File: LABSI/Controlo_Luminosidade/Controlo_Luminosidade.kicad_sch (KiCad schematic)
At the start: 45 parts, among them J1 Barrel_Jack_Switch, J10 Touch Button, J11 Touch Button, J12 Touch Button, J2 Barrel_Jack_Switch, J3 Conn_01x05_Pin, J4 Conn_01x04_Pin, J5 Conn_01x04_Pin, J6 AVR-ISP-6, J7 Conn_01x03_Pin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

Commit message: pcb finalizado, gee«rbers gerados, falta desenvolver o que falta no ultimo commit
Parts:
- added J13: ESP32, Connector_PinSocket_2.54mm:PinSocket_1x04_P2.54mm_Vertical, symbol Connector_Generic:Conn_01x04
- added R8: 6.8k, Resistor_THT:R_Axial_DIN0204_L3.6mm_D1.6mm_P5.08mm_Horizontal, symbol Device:R
- added R9: 10k, Resistor_THT:R_Axial_DIN0204_L3.6mm_D1.6mm_P5.08mm_Horizontal, symbol Device:R
- C9: footprint Capacitor_THT:C_Disc_D3.0mm_W2.0mm_P2.50mm -> (none); now left out of the parts list
- R2: value 330 -> 220
- R4, R5, U2, U3: now left out of the parts list
- U4: footprint Connector_PinHeader_2.54mm:PinHeader_2x02_P2.54mm_Vertical -> Connector_PinSocket_2.54mm:PinSocket_2x02_P2.54mm_Vertical
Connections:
- net +5V: now also J13.3 (Pin_3)
- net GND: now also J13.4 (Pin_4), R9.2
- net TRIG: now also U1.25 (PC2); no longer U1.2 (PD0)
- net TRIG2: now also U1.26 (PC3); no longer U1.3 (PD1)
- net PD5/GATE renamed PB3/GATE
- new net RX_ATMEGA: J13.1 (Pin_1), U1.2 (PD0)
- new net RX_ESP-32: J13.2 (Pin_2), R8.2, R9.1
- new net TX_ATMEGA: R8.1, U1.3 (PD1)
- no-connect marks 8 -> 6
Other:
- note added: "RX-ESP-32- Pin 16 TX-ESP-32- Pin 17"
- moved on the sheet: J10

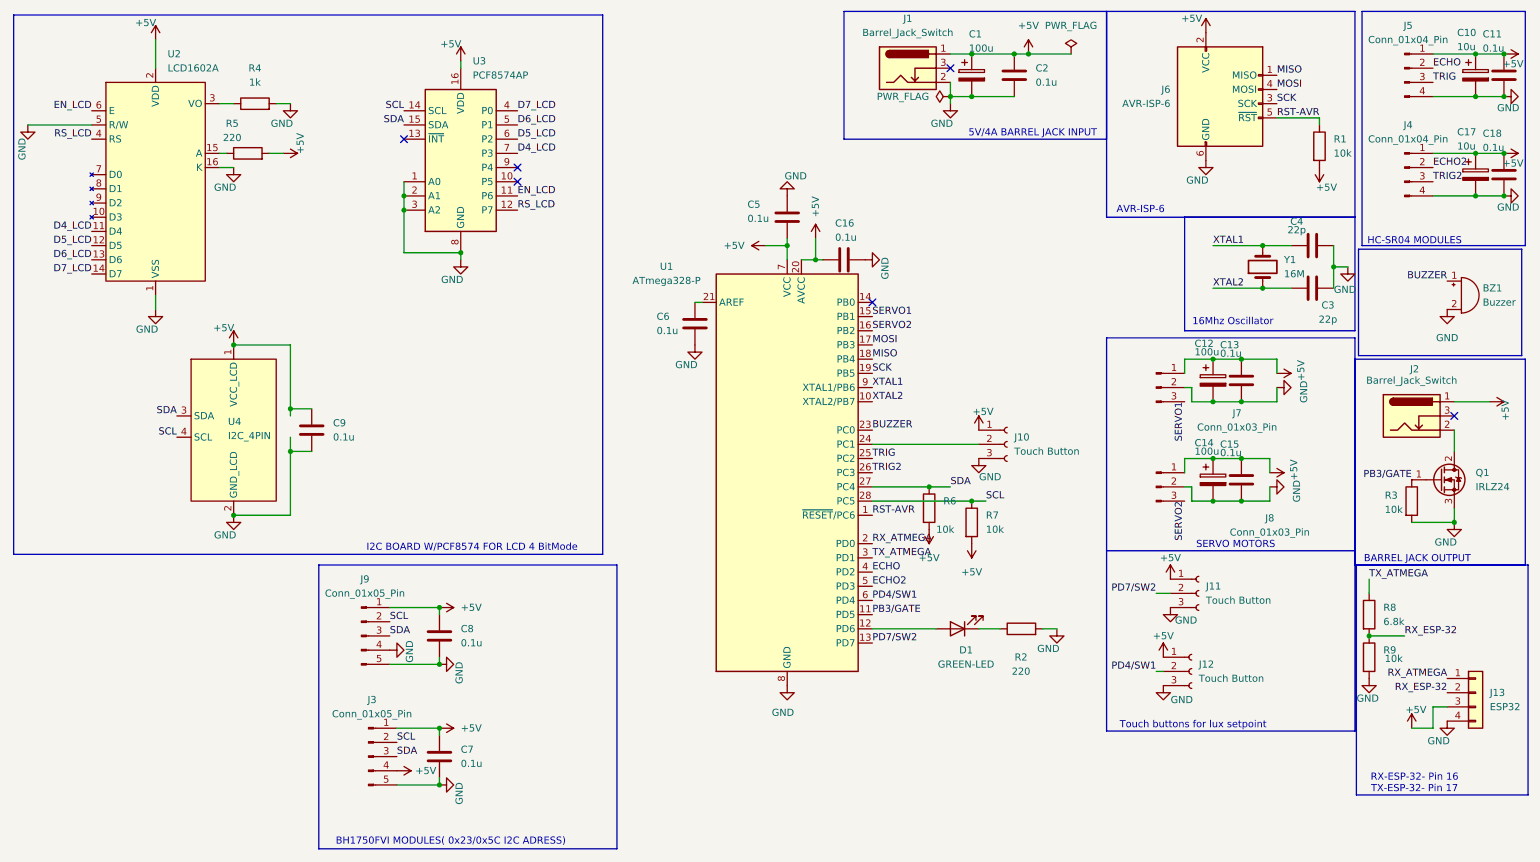
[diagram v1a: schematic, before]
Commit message: pcb mudado, adicionada fusivel de 5A e Diodo tvs na entrada como proteção, gerbers gerados nao foi mexido no firmware
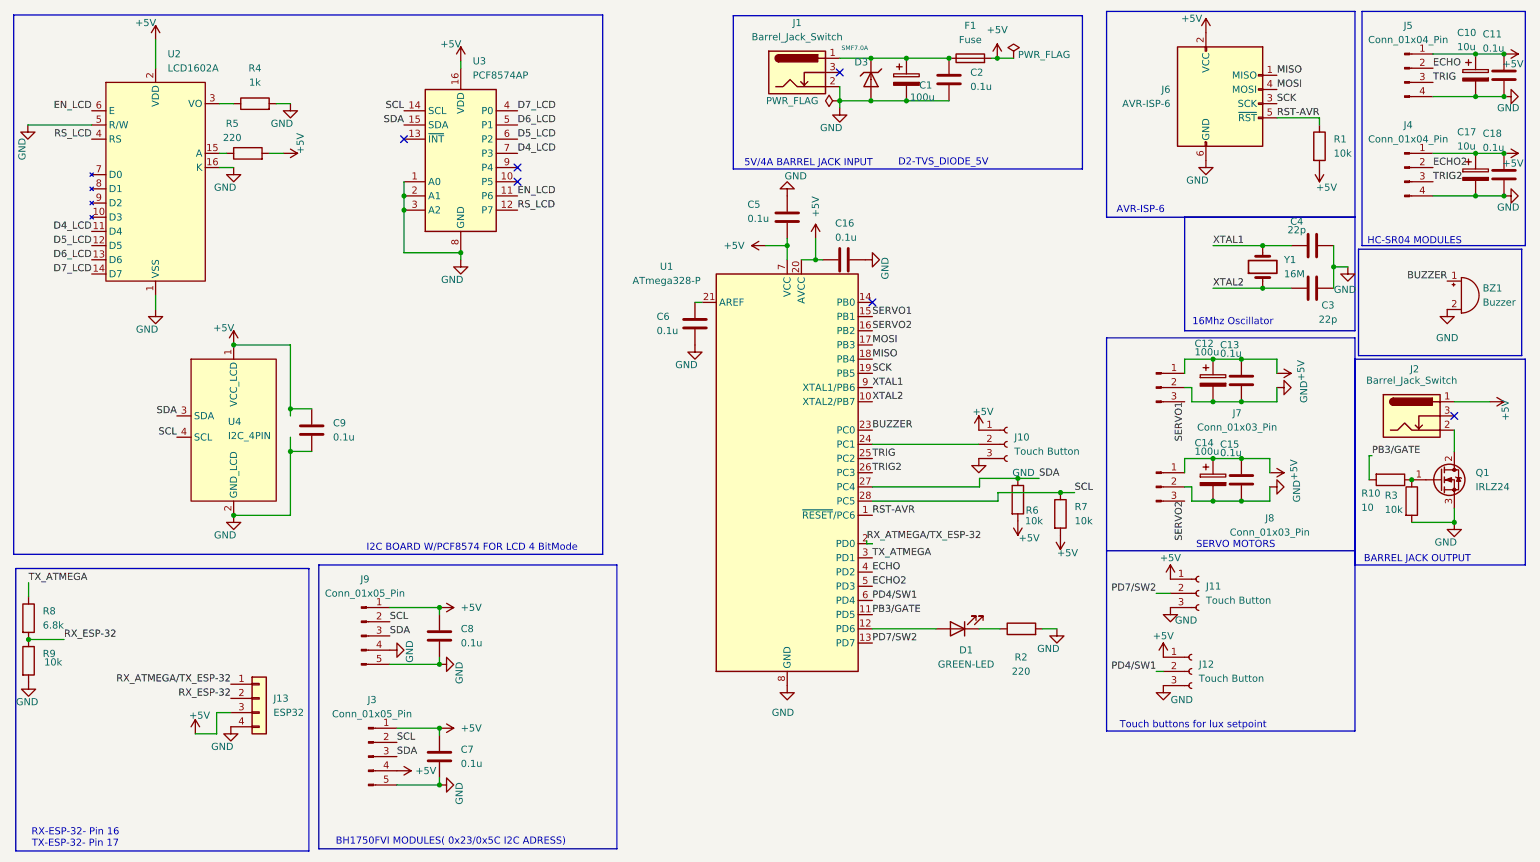
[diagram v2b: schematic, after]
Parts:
- added D3: SMF7.0A, PCM_JLCPCB:D_SOD-123FL, symbol PCM_JLCPCB-Diodes:TVS-Uni,SMF7.0A
- added F1: Fuse, 0ADKP9160-RE:FUSAD2722W65L2250D600, symbol Device:Fuse
- added R10: 10, Resistor_THT:R_Axial_DIN0204_L3.6mm_D1.6mm_P5.08mm_Horizontal, symbol Device:R
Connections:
- net +5V: now also F1.2; no longer C1.1, C2.1, J1.1
- net GND: now also D3.2
- net PB3/GATE: now also R10.2; no longer Q1.1 (G), R3.1
- net RX_ATMEGA renamed RX_ATMEGA/TX_ESP-32
- new net: C1.1, C2.1, D3.1, F1.1, J1.1
- new net: Q1.1 (G), R10.1, R3.1
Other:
- note added: "D2-TVS_DIODE_5V"
- moved on the sheet: C1, C2, J1, J13, R6, R7, R8, R9

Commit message: pcb impresso. falta desenvolver codigo temporizaçao para os motores, trocar codigo display para oled i2c
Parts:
- D3: footprint PCM_JLCPCB:D_SOD-123FL -> PCM_JLCPCB:D_SMA
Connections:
- net +5V: now also C1.1, C2.1, D3.1
- net MOSI: now also R10.2
- net PB3/GATE: no longer names the net of U1.11 (PD5)
- net PB3/GATE: no longer R10.2
- new net: F1.1, J1.1
- no-connect marks 6 -> 7
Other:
- moved on the sheet: C1, C2, D3, F1
